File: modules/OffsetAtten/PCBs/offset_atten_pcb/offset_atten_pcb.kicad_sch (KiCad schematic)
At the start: 8 parts, among them J5 Conn_01x08_Pin, J6 Conn_01x08_Socket, J7 Conn_01x07_Pin, J8 Conn_01x07_Socket

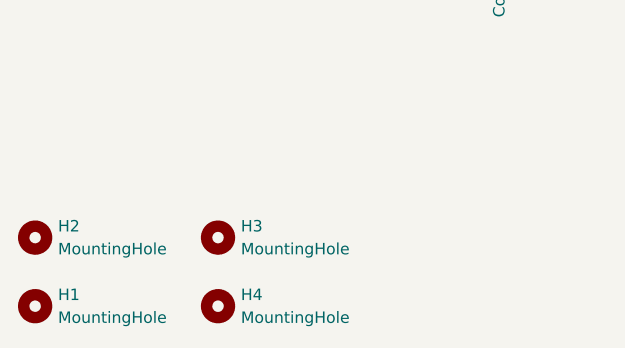
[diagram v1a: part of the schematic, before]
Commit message: Update standoffs in OA PCB
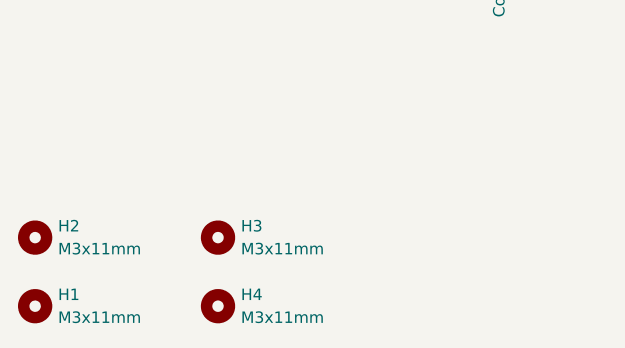
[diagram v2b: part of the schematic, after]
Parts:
- H1, H2, H3, H4: value MountingHole -> M3x11mm; footprint MountingHole:MountingHole_2.7mm_M2.5 -> MountingHole:MountingHole_3.2mm_M3
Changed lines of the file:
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@@
 			)
 		)
-		(property "Value" "MountingHole"
+		(property "Value" "M3x11mm"
 			(at 53.34 153.6699 0)
 			(effects
@@
 			)
 		)
-		(property "Footprint" "MountingHole:MountingHole_2.7mm_M2.5"
+		(property "Footprint" "MountingHole:MountingHole_3.2mm_M3"
 			(at 50.8 152.4 0)
 			(effects
@@
 			)
 		)
-		(property "Value" "MountingHole"
+		(property "Value" "M3x11mm"
 			(at 53.34 146.0499 0)
 			(effects
@@
 			)
 		)
-		(property "Footprint" "MountingHole:MountingHole_2.7mm_M2.5"
+		(property "Footprint" "MountingHole:MountingHole_3.2mm_M3"
 			(at 50.8 144.78 0)
 			(effects
@@
 			)
 		)
-		(property "Value" "MountingHole"
+		(property "Value" "M3x11mm"
 			(at 73.66 153.6699 0)
 			(effects
@@
 			)
 		)
-		(property "Footprint" "MountingHole:MountingHole_2.7mm_M2.5"
+		(property "Footprint" "MountingHole:MountingHole_3.2mm_M3"
 			(at 71.12 152.4 0)
 			(effects
@@
 			)
 		)
-		(property "Value" "MountingHole"
+		(property "Value" "M3x11mm"
 			(at 73.66 146.0499 0)
 			(effects
@@
 			)
 		)
-		(property "Footprint" "MountingHole:MountingHole_2.7mm_M2.5"
+		(property "Footprint" "MountingHole:MountingHole_3.2mm_M3"
 			(at 71.12 144.78 0)
 			(effects

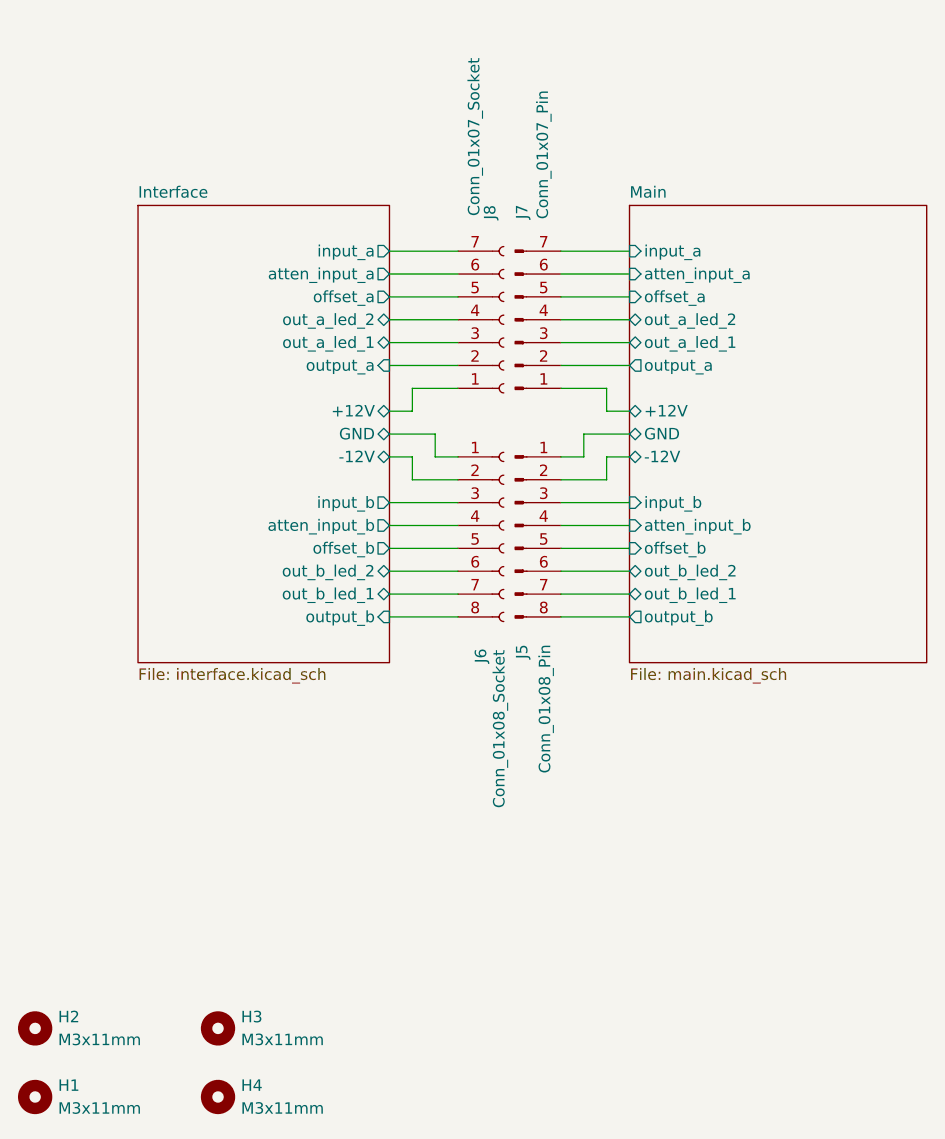
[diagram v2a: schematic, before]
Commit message: Add buffer to O/A; (see #67) closes #62
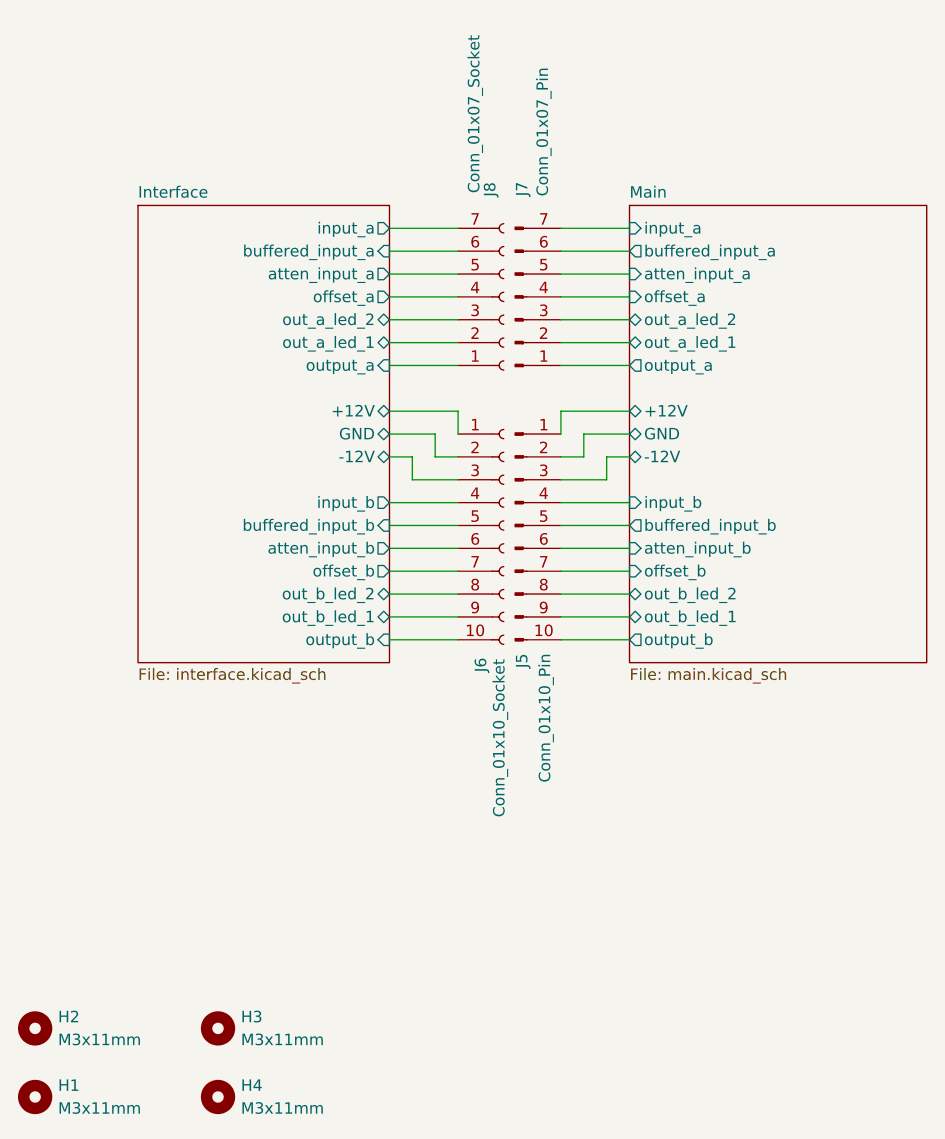
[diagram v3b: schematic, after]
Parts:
- J5: value Conn_01x08_Pin -> Conn_01x10_Pin; footprint Connector_PinSocket_2.54mm:PinSocket_1x08_P2.54mm_Vertical -> Connector_PinSocket_2.54mm:PinSocket_1x10_P2.54mm_Vertical; symbol Connector:Conn_01x08_Pin -> Connector:Conn_01x10_Pin
- J6: value Conn_01x08_Socket -> Conn_01x10_Socket; footprint Connector_PinSocket_2.54mm:PinSocket_1x08_P2.54mm_Vertical -> Connector_PinSocket_2.54mm:PinSocket_1x10_P2.54mm_Vertical; symbol Connector:Conn_01x08_Socket -> Connector:Conn_01x10_Socket
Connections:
- net Interface/+12V: now also J6.1 (Pin_1); no longer J8.1 (Pin_1)
- net Interface/-12V: now also J6.3 (Pin_3); no longer J6.2 (Pin_2)
- net Interface/GND: now also J6.2 (Pin_2); no longer J6.1 (Pin_1)
- net Interface/atten_input_a: now also J8.5 (Pin_5); no longer J8.6 (Pin_6)
- net Interface/atten_input_b: now also J6.6 (Pin_6); no longer J6.4 (Pin_4)
- net Interface/input_b: now also J6.4 (Pin_4); no longer J6.3 (Pin_3)
- net Interface/offset_a: now also J8.4 (Pin_4); no longer J8.5 (Pin_5)
- net Interface/offset_b: now also J6.7 (Pin_7); no longer J6.5 (Pin_5)
- net Interface/out_a_led_1: now also J8.2 (Pin_2); no longer J8.3 (Pin_3)
- net Interface/out_a_led_2: now also J8.3 (Pin_3); no longer J8.4 (Pin_4)
- net Interface/out_b_led_1: now also J6.9 (Pin_9); no longer J6.7 (Pin_7)
- net Interface/out_b_led_2: now also J6.8 (Pin_8); no longer J6.6 (Pin_6)
- net Interface/output_a: now also J8.1 (Pin_1); no longer J8.2 (Pin_2)
- net Interface/output_b: now also J6.10 (Pin_10); no longer J6.8 (Pin_8)
- net Main/+12V: now also J5.1 (Pin_1); no longer J7.1 (Pin_1)
- net Main/-12V: now also J5.3 (Pin_3); no longer J5.2 (Pin_2)
- net Main/GND: now also J5.2 (Pin_2); no longer J5.1 (Pin_1)
- net Main/atten_input_a: now also J7.5 (Pin_5); no longer J7.6 (Pin_6)
- net Main/atten_input_b: now also J5.6 (Pin_6); no longer J5.4 (Pin_4)
- net Main/input_b: now also J5.4 (Pin_4); no longer J5.3 (Pin_3)
- net Main/offset_a: now also J7.4 (Pin_4); no longer J7.5 (Pin_5)
- net Main/offset_b: now also J5.7 (Pin_7); no longer J5.5 (Pin_5)
- net Main/out_a_led_1: now also J7.2 (Pin_2); no longer J7.3 (Pin_3)
- net Main/out_a_led_2: now also J7.3 (Pin_3); no longer J7.4 (Pin_4)
- net Main/out_b_led_1: now also J5.9 (Pin_9); no longer J5.7 (Pin_7)
- net Main/out_b_led_2: now also J5.8 (Pin_8); no longer J5.6 (Pin_6)
- net Main/output_a: now also J7.1 (Pin_1); no longer J7.2 (Pin_2)
- net Main/output_b: now also J5.10 (Pin_10); no longer J5.8 (Pin_8)
- new net Interface/buffered_input_a: J8.6 (Pin_6)
- new net Interface/buffered_input_b: J6.5 (Pin_5)
- new net Main/buffered_input_a: J7.6 (Pin_6)
- new net Main/buffered_input_b: J5.5 (Pin_5)
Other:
- sheet Interface ports: added buffered_input_a, buffered_input_b; removed none
- sheet Main ports: added buffered_input_a, buffered_input_b; removed none
- moved on the sheet: J7, J8
